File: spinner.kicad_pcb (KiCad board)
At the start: 2 copper layers, 190 x 190 mm, 134 parts, among them J1 Micro_SD_Card, SW101 SW_SPDT, U101 SFH617A-3X006, U102 SFH617A-3X006, U103 SFH617A-3X006, U104 RS0102, U105 AP63205WU

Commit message: Adding the FINAL version (final_01_A_REAL_FINAL).  V2
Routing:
- net /OPTO_in_0: track 179.0 -> 180.9 mm
- net /spi_in: track 51.6 -> 50.7 mm, vias 0 -> 1
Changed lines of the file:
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@@
     (fp_line (start -28 -7.54) (end -28 7.66) (layer "F.SilkS") (width 0.12))
     (fp_arc (start 9.8 -7.54) (mid 9.214214 -6.125786) (end 7.8 -5.54) (layer "F.SilkS") (width 0.12))
-    (fp_arc (start -8 -5.54) (mid -9.414214 -6.125786) (end -10 -7.54) (layer "F.SilkS") (width 0.12))
+    (fp_arc (start -8 -5.54) (mid -9.414214 -6.125787) (end -10 -7.54) (layer "F.SilkS") (width 0.12))
     (fp_arc (start 7.8 5.66) (mid 9.214214 6.245786) (end 9.8 7.66) (layer "F.SilkS") (width 0.12))
-    (fp_arc (start -10 7.66) (mid -9.414214 6.245786) (end -8 5.66) (layer "F.SilkS") (width 0.12))
+    (fp_arc (start -10 7.66) (mid -9.414213 6.245786) (end -8 5.66) (layer "F.SilkS") (width 0.12))
     (fp_line (start -28.85 -8.64) (end 28.65 -8.64) (layer "F.CrtYd") (width 0.05))
     (fp_line (start 28.65 -8.64) (end 28.65 8.76) (layer "F.CrtYd") (width 0.05))
@@
     (fp_line (start 22.21 -2) (end 22.21 2) (layer "F.SilkS") (width 0.12))
     (fp_arc (start 9.8 -7.54) (mid 9.214214 -6.125786) (end 7.8 -5.54) (layer "F.SilkS") (width 0.12))
-    (fp_arc (start -10 7.66) (mid -9.414214 6.245786) (end -8 5.66) (layer "F.SilkS") (width 0.12))
+    (fp_arc (start -10 7.66) (mid -9.414213 6.245786) (end -8 5.66) (layer "F.SilkS") (width 0.12))
     (fp_arc (start 7.8 5.66) (mid 9.214214 6.245786) (end 9.8 7.66) (layer "F.SilkS") (width 0.12))
-    (fp_arc (start -8 -5.54) (mid -9.414214 -6.125786) (end -10 -7.54) (layer "F.SilkS") (width 0.12))
+    (fp_arc (start -8 -5.54) (mid -9.414214 -6.125787) (end -10 -7.54) (layer "F.SilkS") (width 0.12))
     (fp_line (start -28.85 -8.64) (end 28.65 -8.64) (layer "F.CrtYd") (width 0.05))
     (fp_line (start -28.85 8.76) (end -28.85 -8.64) (layer "F.CrtYd") (width 0.05))
@@
     (fp_line (start 28.52 -8.505) (end 28.52 8.625) (layer "F.SilkS") (width 0.12))
     (fp_line (start 28.52 8.625) (end -28.72 8.625) (layer "F.SilkS") (width 0.12))
-    (fp_arc (start -10 7.66) (mid -9.414214 6.245786) (end -8 5.66) (layer "F.SilkS") (width 0.12))
-    (fp_arc (start -8 -5.54) (mid -9.414214 -6.125786) (end -10 -7.54) (layer "F.SilkS") (width 0.12))
+    (fp_arc (start -10 7.66) (mid -9.414213 6.245786) (end -8 5.66) (layer "F.SilkS") (width 0.12))
+    (fp_arc (start -8 -5.54) (mid -9.414214 -6.125787) (end -10 -7.54) (layer "F.SilkS") (width 0.12))
     (fp_arc (start 9.8 -7.54) (mid 9.214214 -6.125786) (end 7.8 -5.54) (layer "F.SilkS") (width 0.12))
     (fp_arc (start 7.8 5.66) (mid 9.214214 6.245786) (end 9.8 7.66) (layer "F.SilkS") (width 0.12))
@@
     (fp_arc (start 9.8 -7.54) (mid 9.214214 -6.125786) (end 7.8 -5.54) (layer "F.SilkS") (width 0.12))
     (fp_arc (start 7.8 5.66) (mid 9.214214 6.245786) (end 9.8 7.66) (layer "F.SilkS") (width 0.12))
-    (fp_arc (start -8 -5.54) (mid -9.414214 -6.125786) (end -10 -7.54) (layer "F.SilkS") (width 0.12))
-    (fp_arc (start -10 7.66) (mid -9.414214 6.245786) (end -8 5.66) (layer "F.SilkS") (width 0.12))
+    (fp_arc (start -8 -5.54) (mid -9.414214 -6.125787) (end -10 -7.54) (layer "F.SilkS") (width 0.12))
+    (fp_arc (start -10 7.66) (mid -9.414213 6.245786) (end -8 5.66) (layer "F.SilkS") (width 0.12))
     (fp_line (start 28.65 -8.64) (end 28.65 8.76) (layer "F.CrtYd") (width 0.05))
     (fp_line (start -28.85 -8.64) (end 28.65 -8.64) (layer "F.CrtYd") (width 0.05))
@@
   (segment (start 177.180762 84.122408) (end 179.976915 81.326255) (width 0.25) (layer "B.Cu") (net 17))
   (segment (start 179.976915 81.326255) (end 179.976915 79.921539) (width 0.25) (layer "B.Cu") (net 17))
+  (segment (start 176.67 70.79) (end 176.34 71.12) (width 0.5) (layer "F.Cu") (net 18))
+  (segment (start 176.34 71.12) (end 175.73 71.12) (width 0.5) (layer "F.Cu") (net 18))
   (segment (start 239.5 101.27) (end 235.225 101.27) (width 0.25) (layer "F.Cu") (net 18))
-  (segment (start 171.309999 18.365001) (end 171.309999 47.014999) (width 0.5) (layer "F.Cu") (net 18))
-  (segment (start 171.309999 47.014999) (end 176.67 52.375) (width 0.5) (layer "F.Cu") (net 18))
   (segment (start 182.627846 76.747846) (end 213.057846 76.747846) (width 0.5) (layer "F.Cu") (net 18))
   (segment (start 213.057846 76.747846) (end 229.375 93.065) (width 0.5) (layer "F.Cu") (net 18))
-  (segment (start 175.73 71.12) (end 176.34 71.12) (width 0.5) (layer "F.Cu") (net 18))
+  (segment (start 176.67 54.28) (end 176.67 70.79) (width 0.5) (layer "F.Cu") (net 18))
   (segment (start 231.9 107) (end 227 107) (width 0.5) (layer "F.Cu") (net 18))
-  (segment (start 174.765 14.91) (end 171.309999 18.365001) (width 0.5) (layer "F.Cu") (net 18))
   (segment (start 153.67 71.12) (end 175.73 71.12) (width 0.5) (layer "F.Cu") (net 18))
-  (segment (start 176.67 52.375) (end 176.67 70.79) (width 0.5) (layer "F.Cu") (net 18))
+  (segment (start 169.05 46.66) (end 176.67 54.28) (width 0.5) (layer "F.Cu") (net 18))
   (segment (start 235.06 103.84) (end 231.9 107) (width 0.5) (layer "F.Cu") (net 18))
+  (segment (start 174.765 14.91) (end 169.05 20.625) (width 0.5) (layer "F.Cu") (net 18))
   (segment (start 229.375 93.065) (end 229.375 98.095) (width 0.5) (layer "F.Cu") (net 18))
   (segment (start 232.57 101.29) (end 235.06 101.29) (width 0.5) (layer "F.Cu") (net 18))
@@
   (segment (start 177 71.12) (end 182.627846 76.747846) (width 0.5) (layer "F.Cu") (net 18))
   (segment (start 235.06 101.29) (end 235.06 103.84) (width 0.5) (layer "F.Cu") (net 18))
-  (segment (start 176.34 71.12) (end 176.67 70.79) (width 0.5) (layer "F.Cu") (net 18))
   (segment (start 229.375 98.095) (end 232.57 101.29) (width 0.5) (layer "F.Cu") (net 18))
+  (segment (start 169.05 20.625) (end 169.05 46.66) (width 0.5) (layer "F.Cu") (net 18))
   (segment (start 190.675587 21.930587) (end 190.675587 56.149413) (width 0.5) (layer "F.Cu") (net 19))
   (segment (start 71.26 91.26) (end 71.26 90.16) (width 0.5) (layer "F.Cu") (net 19))
@@
   (segment (start 150.635 35.23) (end 149.365 33.96) (width 0.25) (layer "B.Cu") (net 116))
   (segment (start 142.44 26.11) (end 152.945 26.11) (width 0.25) (layer "F.Cu") (net 117))
-  (segment (start 153.56 28.91) (end 153.56 41.83) (width 0.25) (layer "F.Cu") (net 117))
-  (segment (start 153.56 41.83) (end 151.27 44.12) (width 0.25) (layer "F.Cu") (net 117))
   (segment (start 152.945 26.11) (end 153.56 26.725) (width 0.25) (layer "F.Cu") (net 117))
+  (segment (start 153.56 41.7405) (end 151.27 44.0305) (width 0.25) (layer "F.Cu") (net 117))
   (segment (start 153.56 26.725) (end 153.56 28.91) (width 0.25) (layer "F.Cu") (net 117))
-  (via (at 151.27 44.12) (size 0.8) (drill 0.4) (layers "F.Cu" "B.Cu") (net 117))
-  (segment (start 151.27 44.12) (end 147.32 48.07) (width 0.25) (layer "B.Cu") (net 117))
-  (segment (start 147.32 48.07) (end 147.32 52.07) (width 0.25) (layer "B.Cu") (net 117))
+  (segment (start 153.56 28.91) (end 153.56 41.7405) (width 0.25) (layer "F.Cu") (net 117))
+  (via (at 151.27 44.0305) (size 0.8) (drill 0.4) (layers "F.Cu" "B.Cu") (net 117))
+  (segment (start 147.32 52.07) (end 147.32 47.9805) (width 0.25) (layer "B.Cu") (net 117))
+  (segment (start 147.32 47.9805) (end 151.27 44.0305) (width 0.25) (layer "B.Cu") (net 117))
+  (segment (start 155.76 42.805) (end 153.175 45.39) (width 0.25) (layer "F.Cu") (net 118))
+  (segment (start 150 44.755) (end 148.73 44.755) (width 0.25) (layer "F.Cu") (net 118))
   (segment (start 155.76 28.91) (end 155.76 42.805) (width 0.25) (layer "F.Cu") (net 118))
-  (segment (start 152.54 46.025) (end 144.92 46.025) (width 0.25) (layer "F.Cu") (net 118))
-  (segment (start 144.78 46.165) (end 144.78 52.07) (width 0.25) (layer "F.Cu") (net 118))
   (segment (start 141.645499 24.884501) (end 141.12 25.41) (width 0.25) (layer "F.Cu") (net 118))
   (segment (start 155.76 25.11569) (end 155.528811 24.884501) (width 0.25) (layer "F.Cu") (net 118))
   (segment (start 155.76 28.91) (end 155.76 25.11569) (width 0.25) (layer "F.Cu") (net 118))
-  (segment (start 155.76 42.805) (end 152.54 46.025) (width 0.25) (layer "F.Cu") (net 118))
   (segment (start 155.528811 24.884501) (end 141.645499 24.884501) (width 0.25) (layer "F.Cu") (net 118))
-  (segment (start 144.92 46.025) (end 144.78 46.165) (width 0.25) (layer "F.Cu") (net 118))
+  (segment (start 153.175 45.39) (end 150.635 45.39) (width 0.25) (layer "F.Cu") (net 118))
+  (segment (start 150.635 45.39) (end 150 44.755) (width 0.25) (layer "F.Cu") (net 118))
   (segment (start 141.12 25.41) (end 141.12 26.11) (width 0.25) (layer "F.Cu") (net 118))
+  (via (at 148.73 44.755) (size 0.8) (drill 0.2) (layers "F.Cu" "B.Cu") (net 118))
+  (segment (start 144.78 52.07) (end 144.78 48.705) (width 0.25) (layer "B.Cu") (net 118))
+  (segment (start 144.78 48.705) (end 148.73 44.755) (width 0.25) (layer "B.Cu") (net 118))
   (segment (start 150.5455 26.8855) (end 146.7355 26.8855) (width 0.25) (layer "F.Cu") (net 119))
   (segment (start 151.36 28.91) (end 151.36 27.7) (width 0.25) (layer "F.Cu") (net 119))

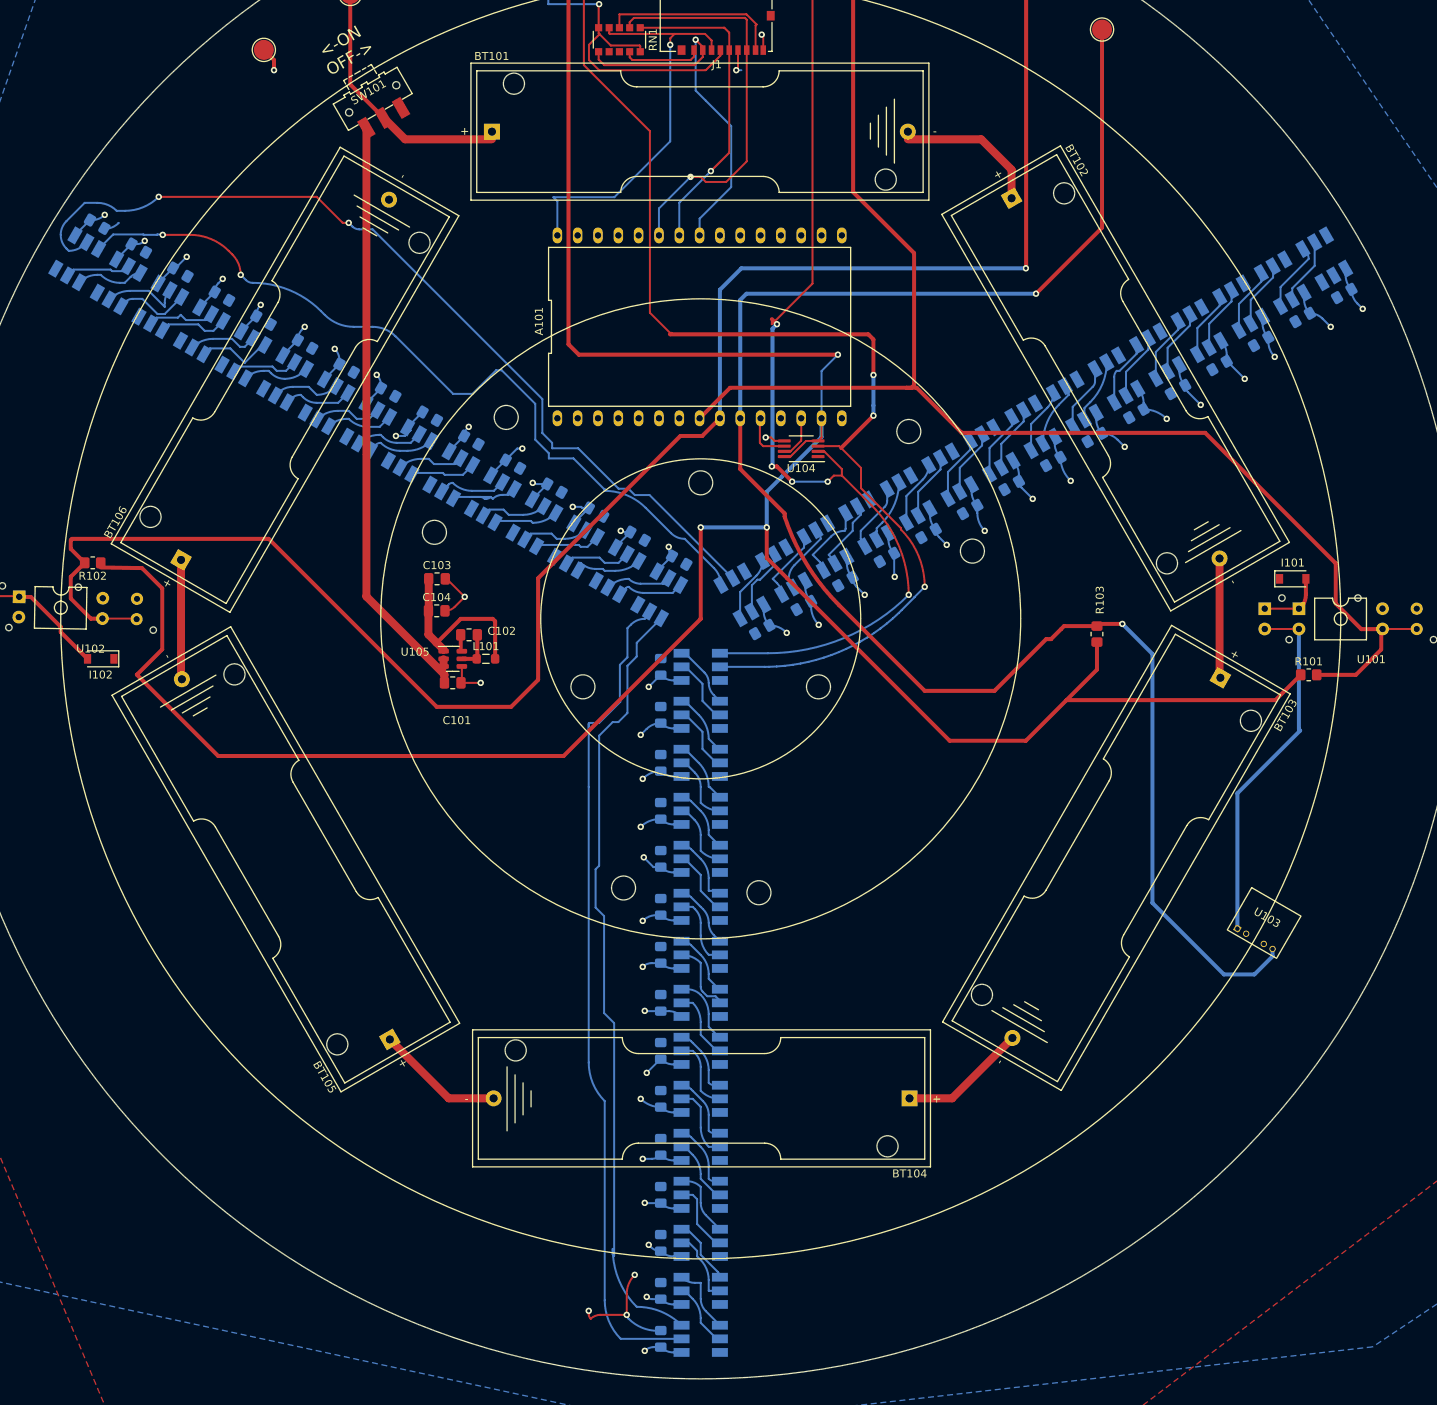
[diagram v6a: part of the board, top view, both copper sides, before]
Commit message: Start the mini version of the spinner.
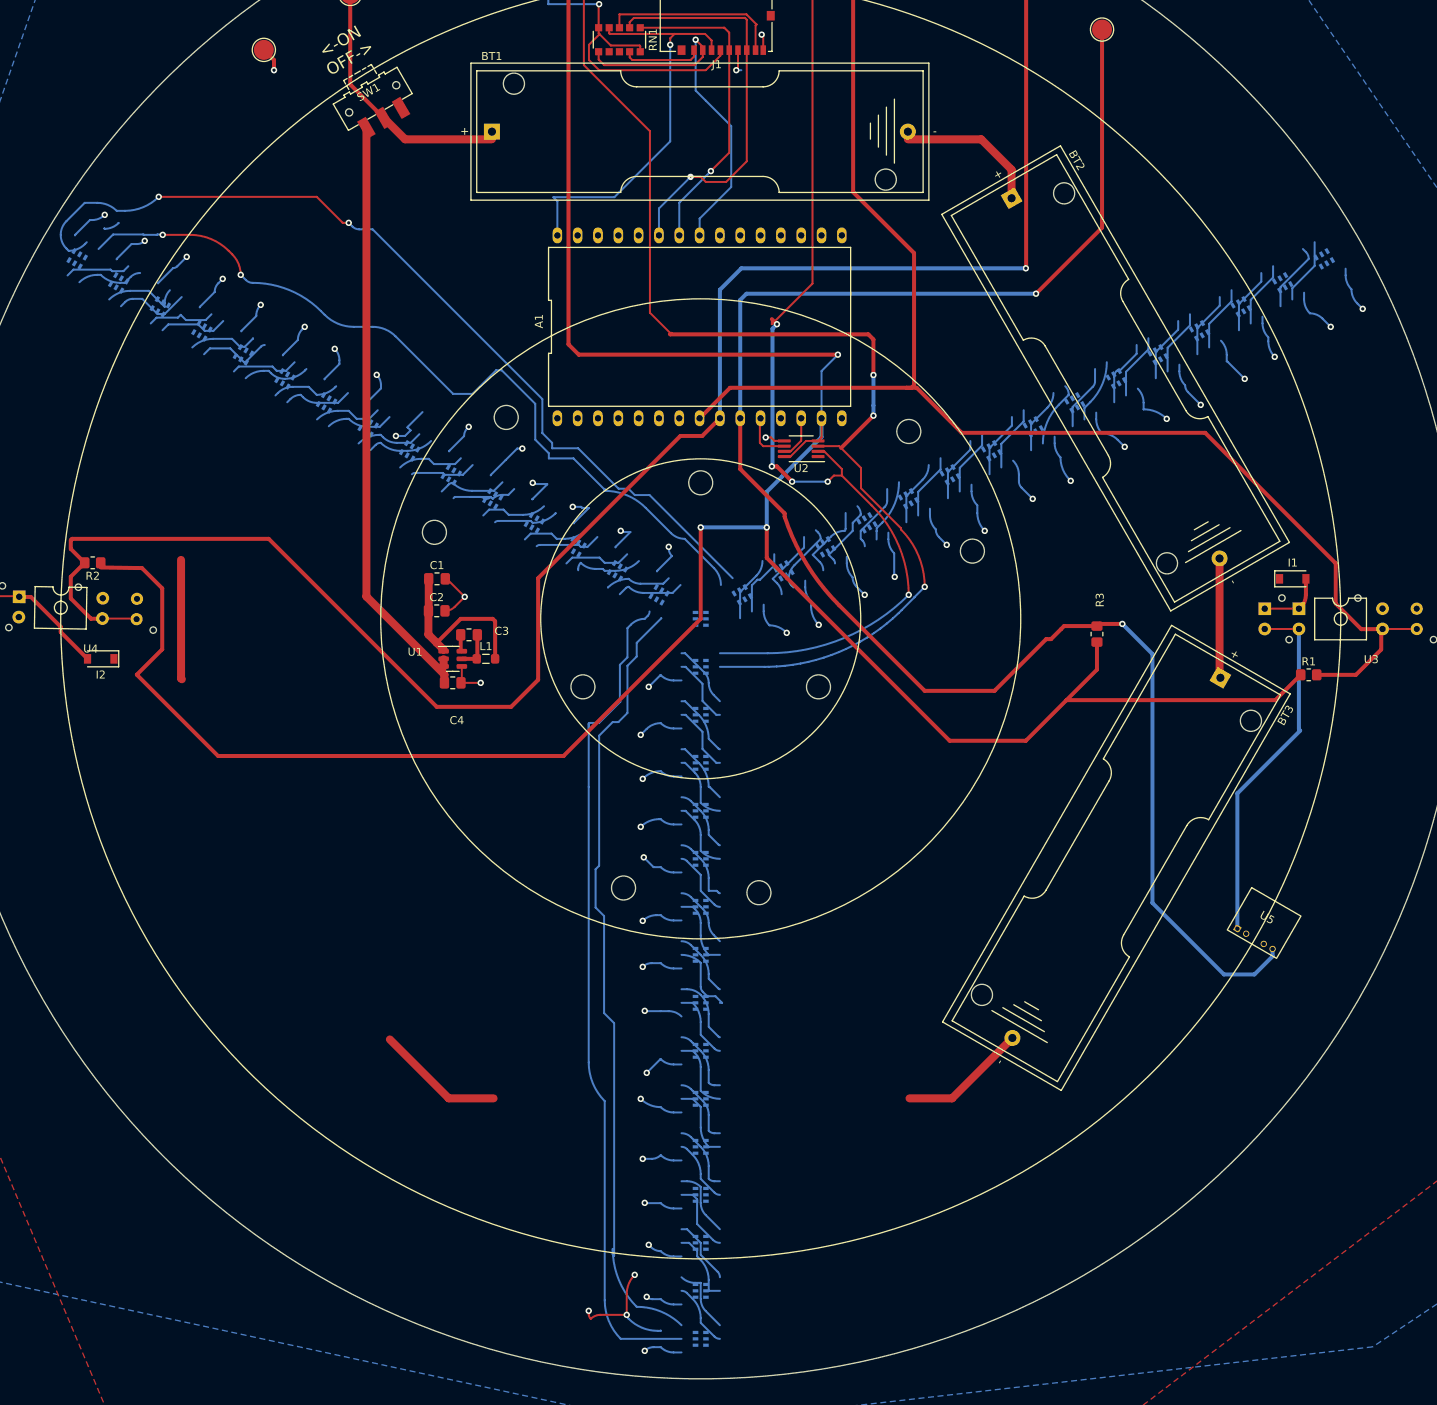
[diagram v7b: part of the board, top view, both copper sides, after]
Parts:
- removed BT104, BT105, BT106: Battery_Cell, Library:Spinner_BatteryHolder_Keystone_2460_1xAA
- removed C105, C106, C107, C108, C109, C110, C111, C112, C113, C114, C115, C116, C117, C118, C119, C120, C121, C122, C123, C124, C125, C126, C127, C128, C129, C130, C131, C132, C133, C134, C135, C136, C137, C138, C139, C140, C141, C142, C143, C144, C145, C146, C147, C148, C149: .1uF, Capacitor_SMD:C_0805_2012Metric_Pad1.18x1.45mm_HandSolder
- added D101: APA102, Library:SK9822-hakz, B.Cu at (150.0, 100.0)
- D0: renamed from D102; footprint LED_SMD:LED_RGB_5050-6 -> Library:SK9822-hakz
- D102: renamed from D105; footprint LED_SMD:LED_RGB_5050-6 -> Library:SK9822-hakz
- D103: renamed from D108; footprint LED_SMD:LED_RGB_5050-6 -> Library:SK9822-hakz
- D104: renamed from D111; footprint LED_SMD:LED_RGB_5050-6 -> Library:SK9822-hakz
- D105: renamed from D114; footprint LED_SMD:LED_RGB_5050-6 -> Library:SK9822-hakz
- D106: renamed from D117; footprint LED_SMD:LED_RGB_5050-6 -> Library:SK9822-hakz
- D107: renamed from D120; footprint LED_SMD:LED_RGB_5050-6 -> Library:SK9822-hakz
- D108: renamed from D123; footprint LED_SMD:LED_RGB_5050-6 -> Library:SK9822-hakz
- D109: renamed from D126; footprint LED_SMD:LED_RGB_5050-6 -> Library:SK9822-hakz
- D110: renamed from D129; footprint LED_SMD:LED_RGB_5050-6 -> Library:SK9822-hakz
- D111: renamed from D132; footprint LED_SMD:LED_RGB_5050-6 -> Library:SK9822-hakz
- D112: renamed from D135; footprint LED_SMD:LED_RGB_5050-6 -> Library:SK9822-hakz
- D113: renamed from D138; footprint LED_SMD:LED_RGB_5050-6 -> Library:SK9822-hakz
- D114: renamed from D141; footprint LED_SMD:LED_RGB_5050-6 -> Library:SK9822-hakz
- D115: renamed from D144; footprint LED_SMD:LED_RGB_5050-6 -> Library:SK9822-hakz
- D201: renamed from D101; footprint LED_SMD:LED_RGB_5050-6 -> Library:SK9822-hakz
- D202: renamed from D104; footprint LED_SMD:LED_RGB_5050-6 -> Library:SK9822-hakz
- D203: renamed from D107; footprint LED_SMD:LED_RGB_5050-6 -> Library:SK9822-hakz
- D204: renamed from D110; footprint LED_SMD:LED_RGB_5050-6 -> Library:SK9822-hakz
- D205: renamed from D113; footprint LED_SMD:LED_RGB_5050-6 -> Library:SK9822-hakz
- D206: renamed from D116; footprint LED_SMD:LED_RGB_5050-6 -> Library:SK9822-hakz
- D207: renamed from D119; footprint LED_SMD:LED_RGB_5050-6 -> Library:SK9822-hakz
- D208: renamed from D122; footprint LED_SMD:LED_RGB_5050-6 -> Library:SK9822-hakz
- D209: renamed from D125; footprint LED_SMD:LED_RGB_5050-6 -> Library:SK9822-hakz
- D210: renamed from D128; footprint LED_SMD:LED_RGB_5050-6 -> Library:SK9822-hakz
- D211: renamed from D131; footprint LED_SMD:LED_RGB_5050-6 -> Library:SK9822-hakz
- D212: renamed from D134; footprint LED_SMD:LED_RGB_5050-6 -> Library:SK9822-hakz
- D213: renamed from D137; footprint LED_SMD:LED_RGB_5050-6 -> Library:SK9822-hakz
- D214: renamed from D140; footprint LED_SMD:LED_RGB_5050-6 -> Library:SK9822-hakz
- D215: renamed from D143; footprint LED_SMD:LED_RGB_5050-6 -> Library:SK9822-hakz
- D301: renamed from D103; footprint LED_SMD:LED_RGB_5050-6 -> Library:SK9822-hakz
- D302: renamed from D106; footprint LED_SMD:LED_RGB_5050-6 -> Library:SK9822-hakz
- D303: renamed from D109; footprint LED_SMD:LED_RGB_5050-6 -> Library:SK9822-hakz
- D304: renamed from D112; footprint LED_SMD:LED_RGB_5050-6 -> Library:SK9822-hakz
- D305: renamed from D115; footprint LED_SMD:LED_RGB_5050-6 -> Library:SK9822-hakz
- D306: renamed from D118; footprint LED_SMD:LED_RGB_5050-6 -> Library:SK9822-hakz
- D307: renamed from D121; footprint LED_SMD:LED_RGB_5050-6 -> Library:SK9822-hakz
- D308: renamed from D124; footprint LED_SMD:LED_RGB_5050-6 -> Library:SK9822-hakz
- D309: renamed from D127; footprint LED_SMD:LED_RGB_5050-6 -> Library:SK9822-hakz
- D310: renamed from D130; footprint LED_SMD:LED_RGB_5050-6 -> Library:SK9822-hakz
- D311: renamed from D133; footprint LED_SMD:LED_RGB_5050-6 -> Library:SK9822-hakz
- D312: renamed from D136; footprint LED_SMD:LED_RGB_5050-6 -> Library:SK9822-hakz
- D313: renamed from D139; footprint LED_SMD:LED_RGB_5050-6 -> Library:SK9822-hakz
- D314: renamed from D142; footprint LED_SMD:LED_RGB_5050-6 -> Library:SK9822-hakz
- D315: renamed from D145; footprint LED_SMD:LED_RGB_5050-6 -> Library:SK9822-hakz
- renumbered A101 to A1, BT101 to BT1, BT102 to BT2, BT103 to BT3, C103 to C1, C104 to C2, C102 to C3, C101 to C4, H101 to H1, H105 to H2, H102 to H3, H106 to H4, H103 to H5, H107 to H6, H104 to H7, H108 to H8, H109 to H9, I101 to I1, I102 to I2, L101 to L1, R101 to R1, R102 to R2, R103 to R3, SW101 to SW1, TP8 to TP1, TP1 to TP2, TP2 to TP3, TP7 to TP5, TP9 to TP6, TP3 to TP7, TP6 to TP8, TP5 to TP9, U105 to U1, U104 to U2, U101 to U3, U102 to U4, U103 to U5
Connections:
- BT3 pad 2: Net-(BT103-Pad2) -> GND
- D0 pad 5: Net-(D102-Pad5) (its old number) -> Net-(D0-Pad5)
- D0 pad 6: Net-(D102-Pad6) (its old number) -> Net-(D0-Pad6)
- D102 pad 1: Net-(D102-Pad6) (its old number) -> Net-(D101-Pad6)
- D102 pad 2: Net-(D102-Pad5) (its old number) -> Net-(D101-Pad5)
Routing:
- net GND: track 39.7 -> 203.5 mm
- net Net-(D214-Pad5): track 8.23 -> 122.8 mm, vias 0 -> 2
- net /CO_3: track 114.3 -> 0.00 mm, vias 2 -> 0
- net VCC: track 254.6 -> 313.1 mm
- net (no net): track 0.00 -> 39.7 mm
- net Net-(D302-Pad6): track 9.15 -> 27.4 mm
- net Net-(D213-Pad6): track 9.59 -> 26.9 mm
- net Net-(D102-Pad5): track 8.54 -> 25.1 mm
- net Net-(BT104-Pad2): track 16.0 -> 0.00 mm
- net Net-(BT103-Pad2): track 16.0 -> 0.00 mm
- net Net-(BT105-Pad2): track 15.0 -> 0.00 mm
- net Net-(D204-Pad6): track 8.05 -> 19.3 mm
- net Net-(D213-Pad5): track 10.3 -> 0.00 mm
- net Net-(D303-Pad6): track 9.79 -> 0.00 mm
- net Net-(D107-Pad5): track 9.60 -> 0.00 mm
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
